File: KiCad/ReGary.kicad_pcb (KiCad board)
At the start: 4 copper layers, 38 x 38 mm, 38 parts, among them J1 Conn_01x02, U1 GW1N-UV1P5LQ100, U2 LM1117-3.3, U3 TPS73643DBV, U4 SN74CBT16210, U5 SN74CBT16210, U6 SN74CBT16210, U7 SN74CBT16210, U8 PLCC_84_plug, U9 PLCC_84_plug

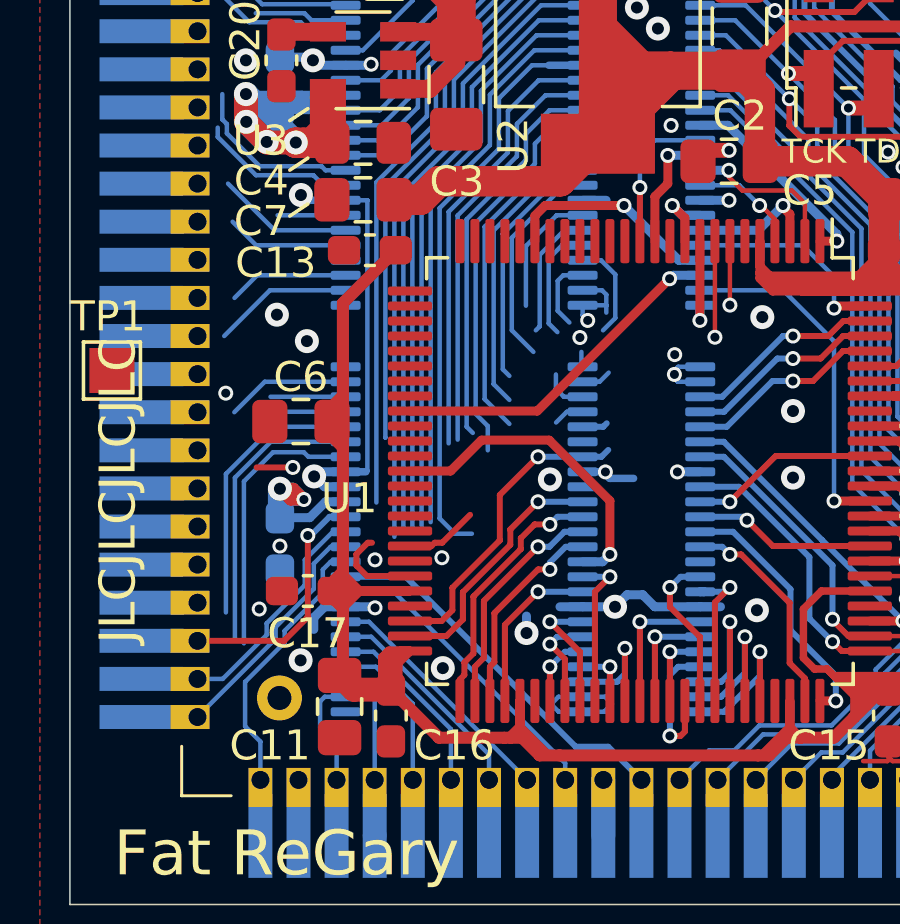
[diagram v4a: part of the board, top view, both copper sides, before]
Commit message: More pin assignments and routing
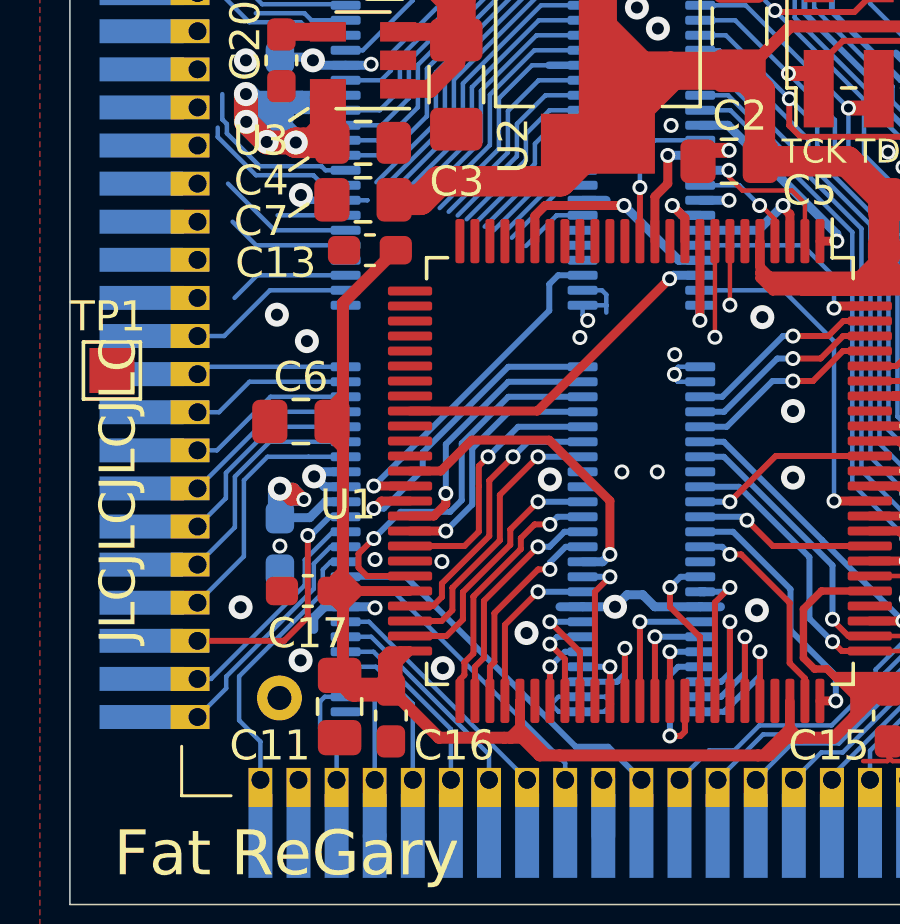
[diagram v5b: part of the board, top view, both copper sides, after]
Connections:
- U1 pad 39: Net-(U1-Pad39) -> FC2_FPGA
- U1 pad 40: Net-(U1-Pad40) -> FC1_FPGA
- U1 pad 41: Net-(U1-Pad41) -> FC0_FPGA
- U1 pad 42: Net-(U1-Pad42) -> RW_FPGA
- U1 pad 43: Net-(U1-Pad43) -> SIZ0_FPGA
- U1 pad 45: Net-(U1-Pad45) -> AS_FPGA
- U1 pad 47: Net-(U1-Pad47) -> SIZ1_FPGA
- U5 pad 2: Net-(U5-Pad2) -> FC2
- U5 pad 46: Net-(U5-Pad46) -> FC2_FPGA
- U7 pad 21: Net-(U7-Pad21) -> RW
- U7 pad 22: Net-(U7-Pad22) -> AS
- U7 pad 23: Net-(U7-Pad23) -> FC0
- U7 pad 24: Net-(U7-Pad24) -> FC1
- U7 pad 25: Net-(U7-Pad25) -> FC1_FPGA
- U7 pad 26: Net-(U7-Pad26) -> FC0_FPGA
- U7 pad 27: Net-(U7-Pad27) -> AS_FPGA
- U7 pad 28: Net-(U7-Pad28) -> RW_FPGA
- U8 pad 22: Net-(U8-Pad22) -> FC2
- U8 pad 23: Net-(U8-Pad23) -> FC1
- U8 pad 24: Net-(U8-Pad24) -> FC0
- U8 pad 25: Net-(U8-Pad25) -> AS
- U8 pad 26: Net-(U8-Pad26) -> RW
- U9 pad 22: Net-(U9-Pad22) -> FC2
- U9 pad 23: Net-(U9-Pad23) -> FC1
- U9 pad 24: Net-(U9-Pad24) -> FC0
- U9 pad 25: Net-(U9-Pad25) -> AS
- U9 pad 26: Net-(U9-Pad26) -> RW
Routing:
- net GND: track 92.3 -> 65.9 mm, vias 45 -> 44
- net AS_FPGA: track 0.00 -> 13.0 mm, vias 0 -> 1
- net FC2_FPGA: track 0.00 -> 11.6 mm, vias 0 -> 1
- net Net-(U5-Pad27): track 21.6 -> 10.0 mm
- net A24_FPGA: track 20.9 -> 9.56 mm
- net A25_FPGA: track 20.2 -> 9.10 mm
- net IENA_FPGA: track 19.5 -> 8.64 mm
- net FC1_FPGA: track 0.00 -> 10.7 mm, vias 0 -> 1
- net Net-(U5-Pad25): track 21.6 -> 10.9 mm
- net A26_FPGA: track 18.8 -> 8.18 mm
- net SIZ1_FPGA: track 0.00 -> 9.37 mm, vias 0 -> 1
- net FC0_FPGA: track 0.00 -> 8.77 mm, vias 0 -> 1
- net RW_FPGA: track 0.00 -> 8.49 mm, vias 0 -> 1
- net Net-(U5-Pad26): track 18.9 -> 10.5 mm
- net SIZ0_FPGA: track 0.85 -> 8.68 mm, vias 0 -> 1
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
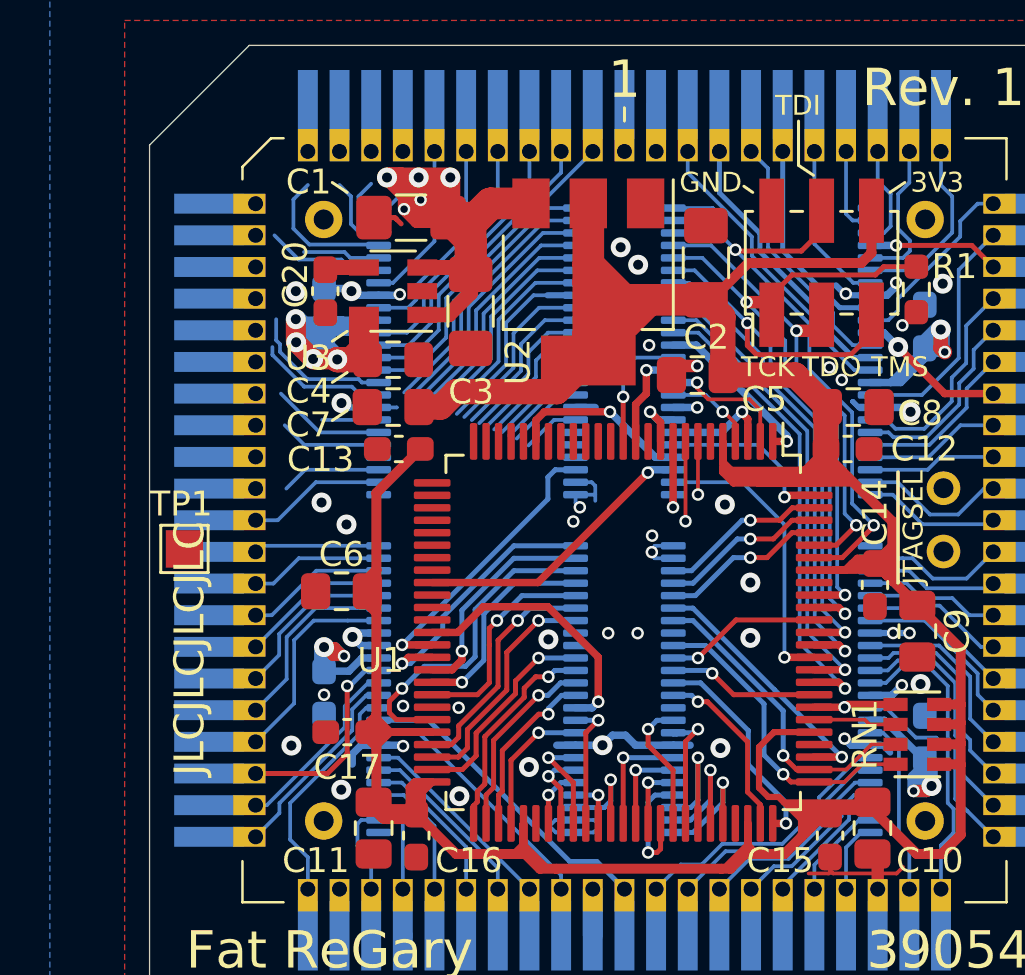
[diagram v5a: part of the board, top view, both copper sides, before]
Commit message: More signals to pin assignments and more routing done
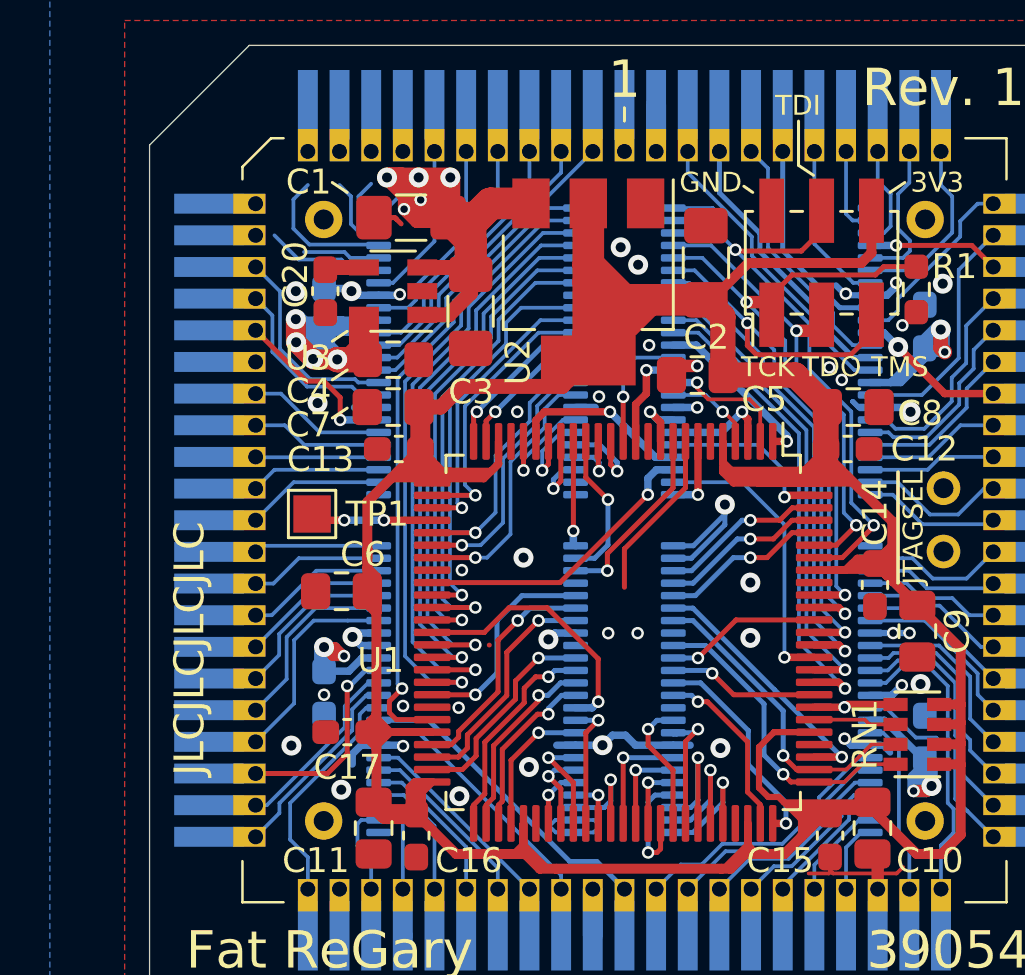
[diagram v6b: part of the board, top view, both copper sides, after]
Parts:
- moved TP1 5.31 mm to (131.9, 74.2)
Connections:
- TP1 pad 1: Net-(TP1-Pad1) -> TP1
- U1 pad 14: Net-(U1-Pad14) -> A1_FPGA
- U1 pad 15: Net-(U1-Pad15) -> A0_FPGA
- U1 pad 16: Net-(U1-Pad16) -> FC0_FPGA
- U1 pad 17: Net-(U1-Pad17) -> FC1_FPGA
- U1 pad 18: Net-(U1-Pad18) -> FC2_FPGA
- U1 pad 19: Net-(U1-Pad19) -> A16_FPGA
- U1 pad 21: Net-(U1-Pad21) -> A17_FPGA
- U1 pad 24: Net-(U1-Pad24) -> A31_FPGA
- U1 pad 25: Net-(U1-Pad25) -> A30_FPGA
- U1 pad 27: Net-(U1-Pad27) -> A29_FPGA
- U1 pad 28: Net-(U1-Pad28) -> A28_FPGA
- U1 pad 29: Net-(U1-Pad29) -> TP1
- U1 pad 30: Net-(U1-Pad30) -> A20_FPGA
- U1 pad 31: Net-(U1-Pad31) -> A19_FPGA
- U1 pad 32: Net-(U1-Pad32) -> A18_FPGA
- U1 pad 35: Net-(U1-Pad35) -> A27_FPGA
- U1 pad 36: Net-(U1-Pad36) -> A26_FPGA
- U1 pad 37: Net-(U1-Pad37) -> A21_FPGA
- U1 pad 39: FC2_FPGA -> A22_FPGA
- U1 pad 40: FC1_FPGA -> A23_FPGA
- U1 pad 41: FC0_FPGA -> A24_FPGA
- U1 pad 42: RW_FPGA -> A25_FPGA
- U1 pad 45: AS_FPGA -> IENA_FPGA
- U1 pad 7: Net-(U1-Pad7) -> ECLK_FPGA
- U1 pad 8: Net-(U1-Pad8) -> RW_FPGA
- U1 pad 9: ECLK_FPGA -> AS_FPGA
- U5 pad 10: Net-(U5-Pad10) -> A20
- U5 pad 19: IENA -> A21
- U5 pad 20: A25 -> A22
- U5 pad 21: A24 -> A23
- U5 pad 22: Net-(U5-Pad22) -> A24
- U5 pad 23: Net-(U5-Pad23) -> A25
- U5 pad 24: Net-(U5-Pad24) -> IENA
- U5 pad 25: Net-(U5-Pad25) -> IENA_FPGA
- U5 pad 26: Net-(U5-Pad26) -> A25_FPGA
- U5 pad 27: Net-(U5-Pad27) -> A24_FPGA
- U5 pad 28: A24_FPGA -> A23_FPGA
- U5 pad 29: A25_FPGA -> A22_FPGA
- U5 pad 3: Net-(U5-Pad3) -> A0
- U5 pad 30: IENA_FPGA -> A21_FPGA
- U5 pad 38: Net-(U5-Pad38) -> A20_FPGA
- U5 pad 39: Net-(U5-Pad39) -> A19_FPGA
- U5 pad 4: Net-(U5-Pad4) -> A1
- U5 pad 40: Net-(U5-Pad40) -> A18_FPGA
- U5 pad 42: Net-(U5-Pad42) -> A17_FPGA
- U5 pad 43: Net-(U5-Pad43) -> A16_FPGA
- U5 pad 44: Net-(U5-Pad44) -> A1_FPGA
- U5 pad 45: Net-(U5-Pad45) -> A0_FPGA
- U5 pad 5: Net-(U5-Pad5) -> A16
- U5 pad 6: Net-(U5-Pad6) -> A17
- U5 pad 7: Net-(U5-Pad7) -> A18
- U5 pad 9: Net-(U5-Pad9) -> A19
- U8 pad 11: Net-(U8-Pad11) -> A23
- U8 pad 12: Net-(U8-Pad12) -> A22
- U8 pad 13: Net-(U8-Pad13) -> A21
- U8 pad 14: Net-(U8-Pad14) -> A20
- U8 pad 15: Net-(U8-Pad15) -> A19
- U8 pad 16: Net-(U8-Pad16) -> A18
- U8 pad 18: Net-(U8-Pad18) -> A17
- U8 pad 19: Net-(U8-Pad19) -> A16
- U8 pad 20: Net-(U8-Pad20) -> A1
- U8 pad 21: Net-(U8-Pad21) -> A0
- U9 pad 11: Net-(U9-Pad11) -> A23
- U9 pad 12: Net-(U9-Pad12) -> A22
- U9 pad 13: Net-(U9-Pad13) -> A21
- U9 pad 14: Net-(U9-Pad14) -> A20
- U9 pad 15: Net-(U9-Pad15) -> A19
- U9 pad 16: Net-(U9-Pad16) -> A18
- U9 pad 18: Net-(U9-Pad18) -> A17
- U9 pad 19: Net-(U9-Pad19) -> A16
- U9 pad 20: Net-(U9-Pad20) -> A1
- U9 pad 21: Net-(U9-Pad21) -> A0
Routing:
- net A23_FPGA: track 0.00 -> 22.0 mm, vias 0 -> 1
- net A22_FPGA: track 0.00 -> 21.9 mm, vias 0 -> 1
- net A21_FPGA: track 0.00 -> 19.3 mm, vias 0 -> 1
- net 3V3: track 184.8 -> 203.6 mm
- net IENA_FPGA: track 8.64 -> 26.0 mm, vias 0 -> 1
- net A25_FPGA: track 9.10 -> 24.9 mm, vias 0 -> 1
- net A24_FPGA: track 9.56 -> 24.6 mm, vias 0 -> 1
- net Net-(U5-Pad25): track 10.9 -> 0.00 mm
- net A26_FPGA: track 8.18 -> 19.0 mm, vias 0 -> 1
- net A18_FPGA: track 0.00 -> 10.6 mm, vias 0 -> 1
- net Net-(U5-Pad26): track 10.5 -> 0.00 mm
- net A19_FPGA: track 0.00 -> 10.4 mm, vias 0 -> 1
- net A20_FPGA: track 0.00 -> 10.2 mm, vias 0 -> 1
- net Net-(U5-Pad27): track 10.0 -> 0.00 mm
- net A27_FPGA: track 7.09 -> 16.3 mm, vias 0 -> 1
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
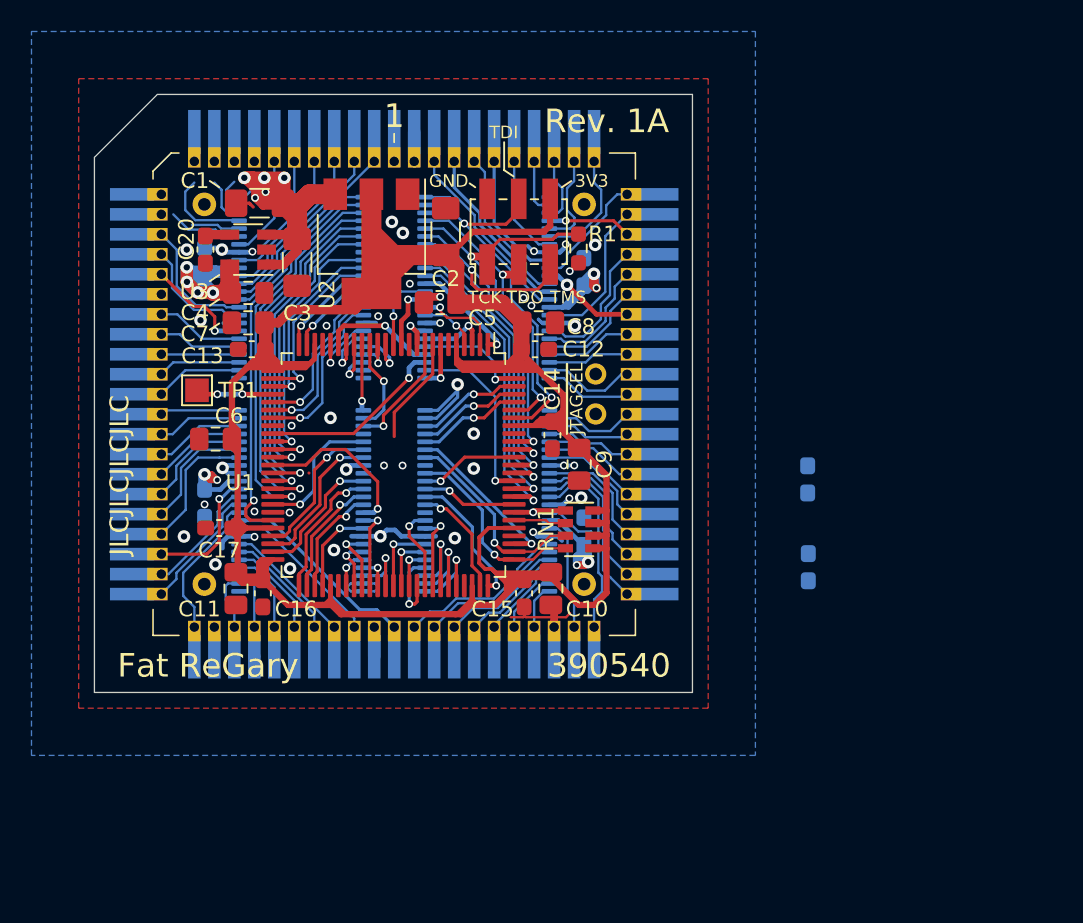
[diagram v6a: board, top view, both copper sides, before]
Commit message: Improved GND by adding/relocating some GND-vias, also more routing fixes done
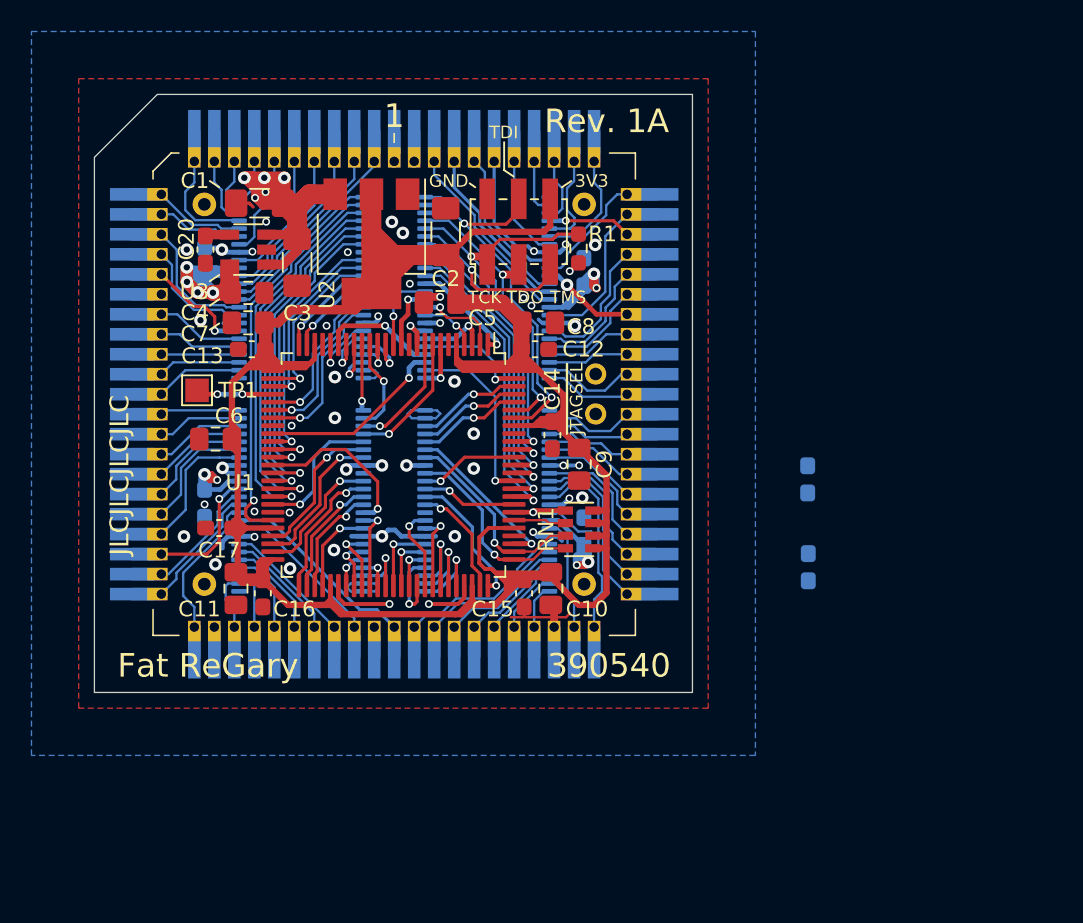
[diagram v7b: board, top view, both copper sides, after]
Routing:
- net GND: track 57.8 -> 74.8 mm, vias 42 -> 47
- net VCC: track 99.1 -> 112.3 mm
- net A22: track 3.09 -> 7.70 mm
- net A24: track 3.02 -> 6.23 mm
- net A23: track 5.69 -> 8.90 mm
- net A25: track 2.37 -> 5.53 mm
- net A21: track 4.76 -> 7.38 mm
- net IENA: track 2.17 -> 4.75 mm
- net KBCLK: track 11.0 -> 12.9 mm
- net A30: track 11.7 -> 13.6 mm
- net RTCRD: track 7.22 -> 9.09 mm
- net CIA0: track 6.55 -> 8.41 mm
- net AVEC: track 7.25 -> 9.12 mm
- net SLOT: track 3.96 -> 5.83 mm
- net A15: track 3.76 -> 5.63 mm
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
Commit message: Fixed enumeration of capacitors and placement of last capacitor C11 for 3V3-power
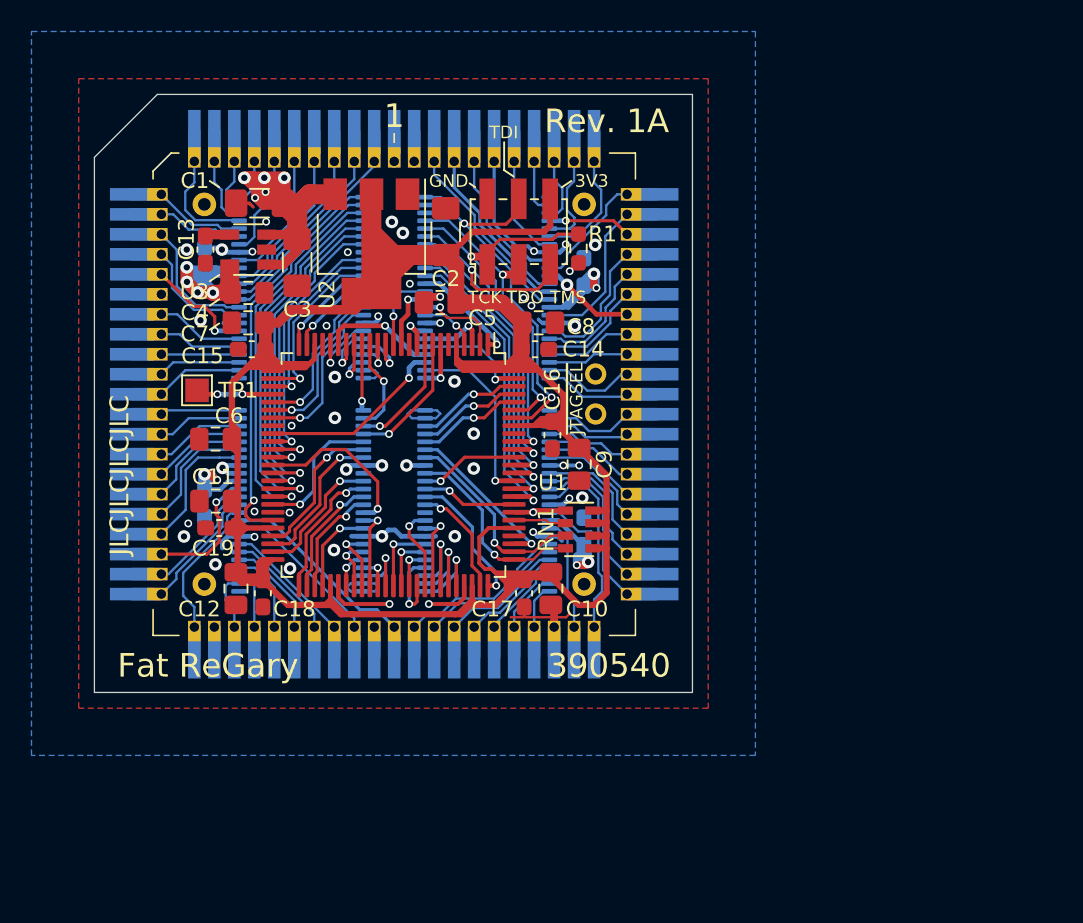
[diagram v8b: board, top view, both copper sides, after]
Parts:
- removed the C17 at (133.3, 83.0)
- removed the C18 at (170.8, 85.4)
- removed the C22 at (132.4, 81.4)
- removed C24: 0.01uF, Capacitor_SMD:C_0603_1608Metric_Pad1.05x0.95mm_HandSolder
- added C11: 0.1uF, Capacitor_SMD:C_0805_2012Metric_Pad1.18x1.45mm_HandSolder, F.Cu at (133.1, 81.2)
- added C21: 0.01uF, Capacitor_SMD:C_0603_1608Metric_Pad1.05x0.95mm_HandSolder, B.Cu at (132.4, 81.4)
- added C23: 0.01uF, Capacitor_SMD:C_0603_1608Metric_Pad1.05x0.95mm_HandSolder, B.Cu at (156.5, 83.2)
- C19: moved to F.Cu
- moved C19 37.5 mm to (133.3, 83.0), turned to 0 degrees
- renumbered C11 to C12, C20 to C13, C12 to C14, C13 to C15, C14 to C16, C15 to C17, C16 to C18, C21 to C20, C23 to C22
